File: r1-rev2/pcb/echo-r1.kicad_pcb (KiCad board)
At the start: 6 copper layers, 55 x 95 mm, 0 parts

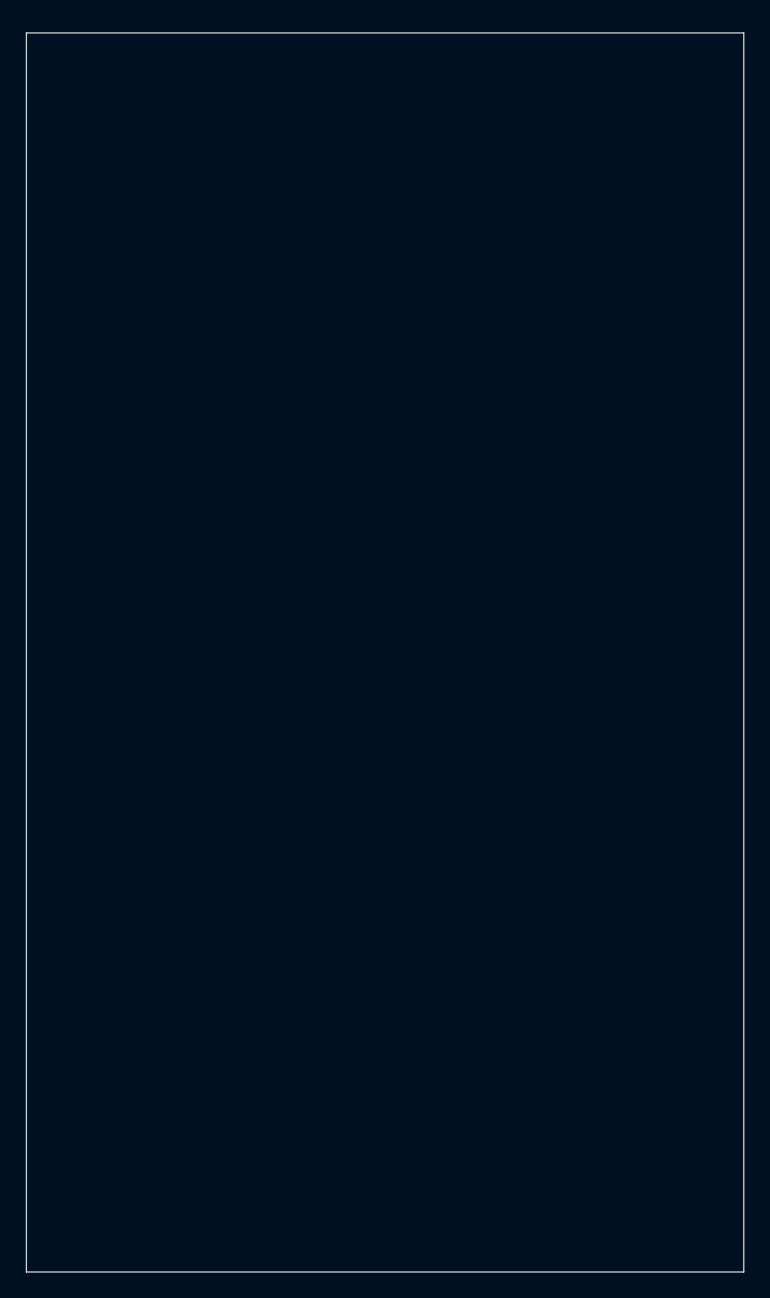
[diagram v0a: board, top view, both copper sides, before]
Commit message: R1-Rev2: update PCB stackup and board outline
The new board stackup uses alternate signal and ground layers,
being careful not to cross thicker cores. This should keep the
electric fields smaller, and in theory, is better for EMI than
the old stackup which didn't pay attention to the space between
layers. Power will be routed on signal layers.

The board outline is now rounded generously for compatibility
with CNC machined cases (which require rounded inner corners).
It is also now toleranced back from the inner edge of the case,
but I may pull it back further still.

There were some minor disreprancies from the intended JLC stackup
which have also been fixed, not that it really matters since KiCAD
doesn't use those values.
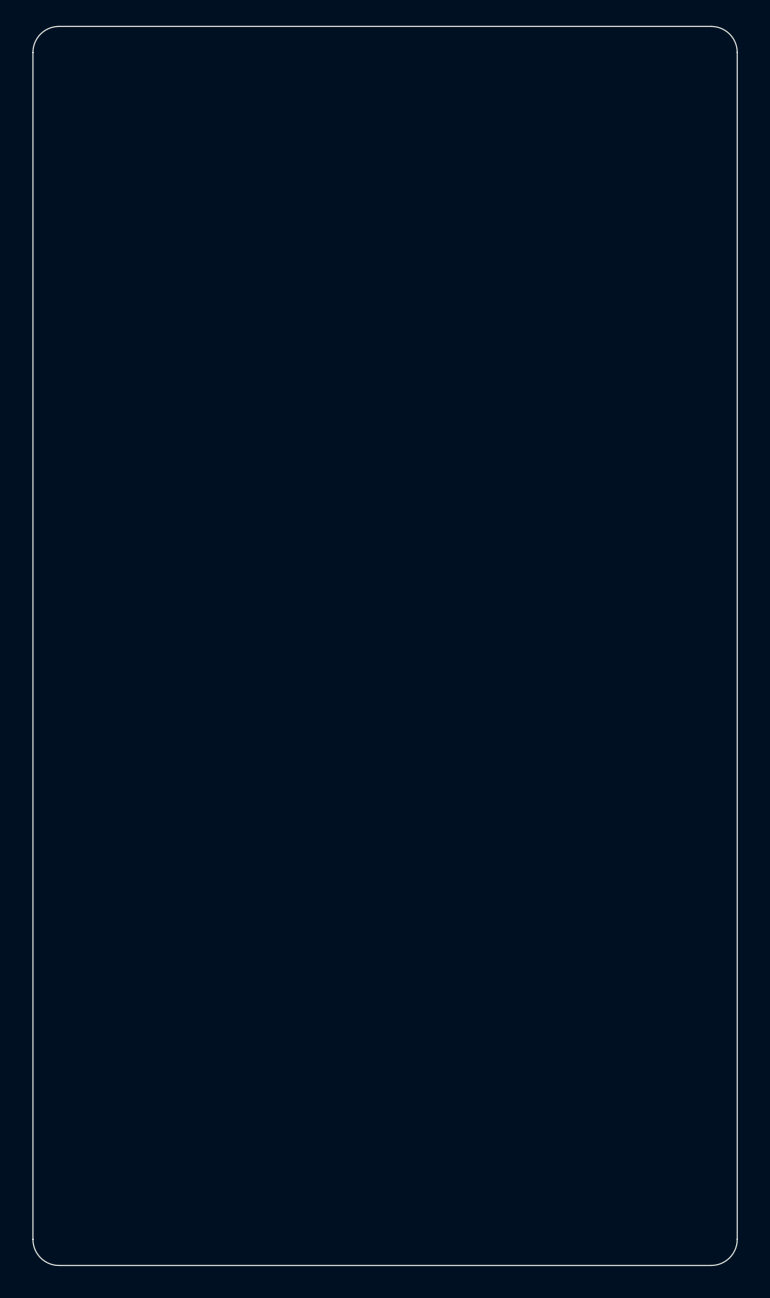
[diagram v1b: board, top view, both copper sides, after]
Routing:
- added copper zone on In2.Cu, net GND
- removed copper zone on In2.Cu, net (none)
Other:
- board size 55 x 95 mm -> 54 x 95 mm
- board text added: "Stackup: JLC06101H-3313, 1mm"
- board text removed: "Stackup: JLC06101H-3313"
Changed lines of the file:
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@@
 	(generator_version "9.0")
 	(general
-		(thickness 1.0524)
+		(thickness 1.06)
 		(legacy_teardrops no)
 	)
 	(paper "A4")
 	(layers
-		(0 "F.Cu" signal)
+		(0 "F.Cu" mixed)
 		(4 "In1.Cu" power "F.Gnd")
-		(6 "In2.Cu" power "F.Pwr")
-		(8 "In3.Cu" mixed "B.Inner")
+		(6 "In2.Cu" power "I.Gnd")
+		(8 "In3.Cu" mixed "I.Cu")
 		(10 "In4.Cu" power "B.Gnd")
-		(2 "B.Cu" signal)
+		(2 "B.Cu" mixed)
 		(9 "F.Adhes" user "F.Adhesive")
 		(11 "B.Adhes" user "B.Adhesive")
@@
 				(thickness 0.0994)
 				(material "3313*1")
-				(epsilon_r 4.5)
+				(epsilon_r 4.1)
 				(loss_tangent 0.02)
 			)
@@
 			(layer "dielectric 3"
 				(type "prepreg")
-				(thickness 0.2028)
+				(thickness 0.2104)
 				(material "7268*1")
 				(epsilon_r 4.5)
@@
 				(thickness 0.0994)
 				(material "3313*1")
-				(epsilon_r 4.5)
+				(epsilon_r 4.1)
 				(loss_tangent 0.02)
 			)
@@
 		(allow_soldermask_bridges_in_footprints no)
 		(tenting front back)
-		(aux_axis_origin 121 152.5)
-		(grid_origin 121 152.5)
+		(aux_axis_origin 121.5 152)
+		(grid_origin 121.5 152)
 		(pcbplotparams
 			(layerselection 0x00000000_00000000_55555555_5755f5ff)
@@
 	(net 1 "GND")
 	(gr_rect
-		(start 118.5 55)
-		(end 178.5 155)
+		(start 121 56.5)
+		(end 176 152.5)
 		(stroke
 			(width 0.1)
-			(type default)
+			(type solid)
 		)
 		(fill no)
@@
 	)
 	(gr_rect
-		(start 121 57.5)
-		(end 176 152.5)
-		(stroke
-			(width 0.05)
-			(type default)
+		(start 118.5 54.5)
+		(end 178.5 154.5)
+		(stroke
+			(width 0.1)
+			(type solid)
 		)
 		(fill no)
-		(layer "Edge.Cuts")
-	)
-	(gr_text "Stackup: JLC06101H-3313"
+		(layer "Dwgs.User")
+	)
+	(gr_arc
+		(start 121.5 59)
+		(mid 122.085786 57.585786)
+		(end 123.5 57)
+		(stroke
+			(width 0.05)
+			(type default)
+		)
+		(layer "Edge.Cuts")
+	)
+	(gr_arc
+		(start 123.5 152)
+		(mid 122.085786 151.414214)
+		(end 121.5 150)
+		(stroke
+			(width 0.05)
+			(type default)
+		)
+		(layer "Edge.Cuts")
+	)
+	(gr_line
+		(start 121.5 59)
+		(end 121.5 150)
+		(stroke
+			(width 0.05)
+			(type default)
+		)
+		(layer "Edge.Cuts")
+	)
+	(gr_line
+		(start 173.5 57)
+		(end 123.5 57)
+		(stroke
+			(width 0.05)
+			(type default)
+		)
+		(layer "Edge.Cuts")
+	)
+	(gr_arc
+		(start 173.5 57)
+		(mid 174.914214 57.585786)
+		(end 175.5 59)
+		(stroke
+			(width 0.05)
+			(type default)
+		)
+		(layer "Edge.Cuts")
+	)
+	(gr_line
+		(start 175.499999 150)
+		(end 175.5 59)
+		(stroke
+			(width 0.05)
+			(type default)
+		)
+		(layer "Edge.Cuts")
+	)
+	(gr_arc
+		(start 175.499999 150)
+		(mid 174.914213 151.414214)
+		(end 173.499999 152)
+		(stroke
+			(width 0.05)
+			(type default)
+		)
+		(layer "Edge.Cuts")
+	)
+	(gr_line
+		(start 123.5 152)
+		(end 173.5 152)
+		(stroke
+			(width 0.05)
+			(type default)
+		)
+		(layer "Edge.Cuts")
+	)
+	(gr_text "Stackup: JLC06101H-3313, 1mm"
 		(at 118.75 53.5 0)
 		(layer "Cmts.User")
@@
 		(net 1)
 		(net_name "GND")
-		(layers "In1.Cu" "In4.Cu")
+		(layers "In1.Cu" "In2.Cu" "In4.Cu")
 		(hatch edge 0.5)
 		(priority 1)
@@
 		(polygon
 			(pts
-				(xy 121 57.5) (xy 176 57.5) (xy 176 152.5) (xy 121 152.5)
-			)
-		)
-	)
-	(zone
-		(net 0)
-		(net_name "")
-		(layer "In2.Cu")
-		(hatch edge 0.5)
-		(priority 14)
-		(connect_pads yes
-			(clearance 0.25)
-		)
-		(min_thickness 0.25)
-		(filled_areas_thickness no)
-		(fill
-			(thermal_gap 0.5)
-			(thermal_bridge_width 0.5)
-		)
-		(polygon
-			(pts
-				(xy 121 57.5) (xy 176 57.5) (xy 176 152.5) (xy 121 152.5)
-			)
-		)
+				(xy 121.5 57) (xy 175.5 57) (xy 175.5 152) (xy 121.5 152)
+			)
+		)

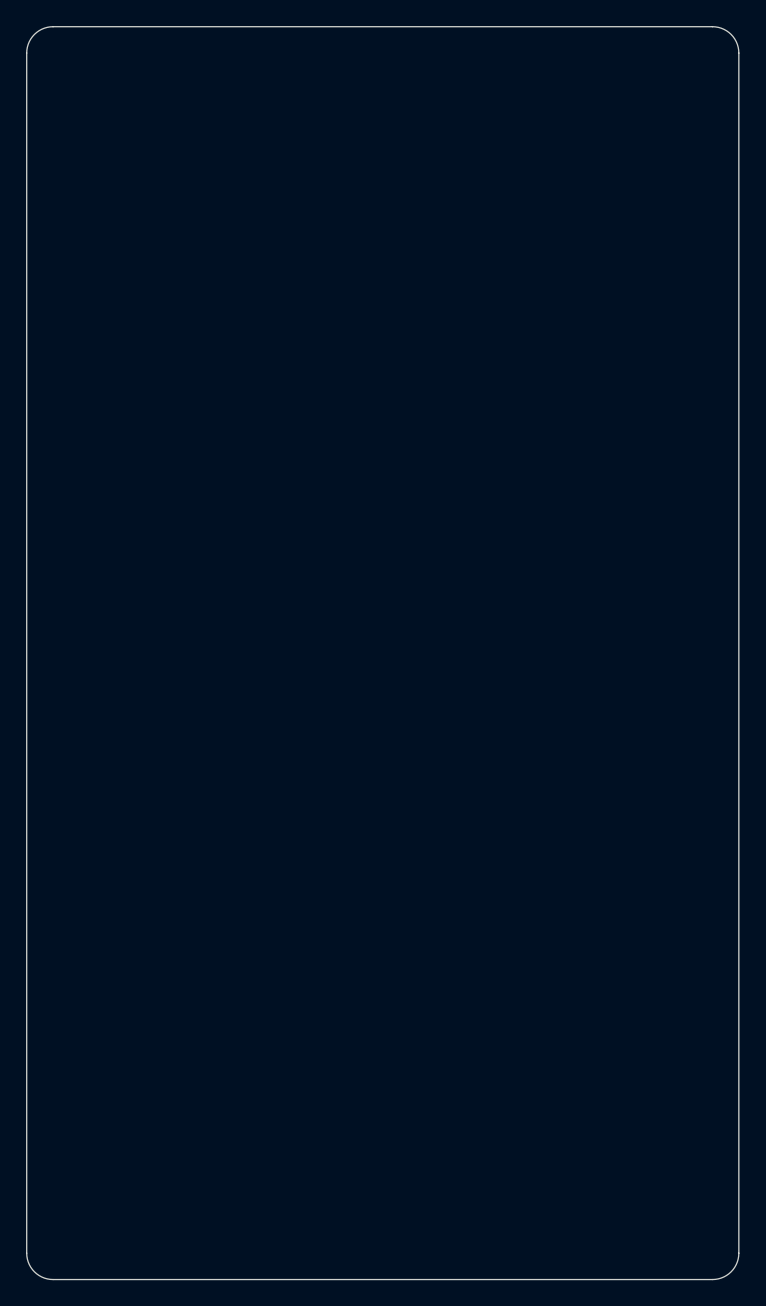
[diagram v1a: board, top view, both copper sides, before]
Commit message: R1-Rev2: initial mechanical layout
- Outline front side of case, LCD module, and cable
- Lay out LCD, since it requires 12'oclock viewing angle a slot is
  required to thread the ribbon cable through to the back plane.
- Place buttons, HP/LO jacks, and USB port
- Make the power/volume buttons larger
- Remove old button footprints
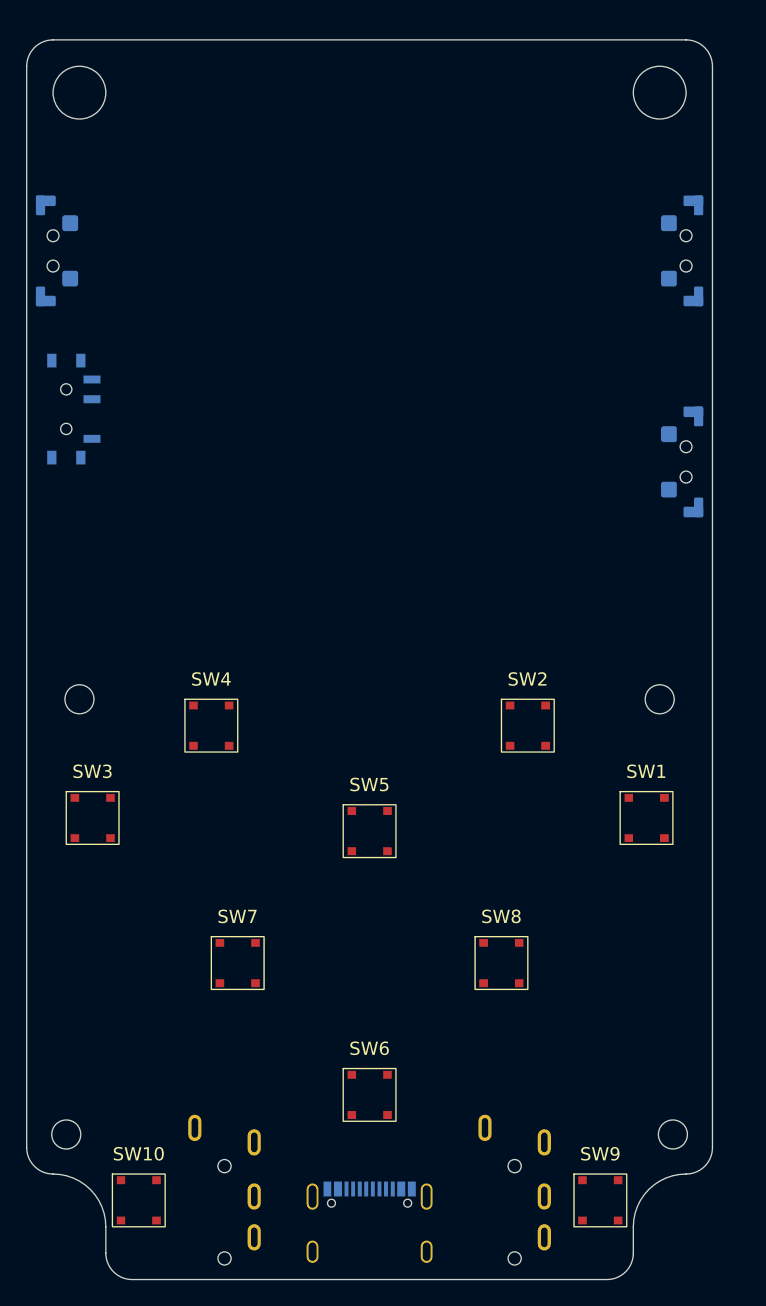
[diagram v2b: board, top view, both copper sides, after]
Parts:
- added H1: M2x2mm, MountingHole:MountingHole_2.2mm_M2, B.Cu at (125.5, 108.0)
- added H2: M2x2mm, MountingHole:MountingHole_2.2mm_M2, B.Cu at (169.5, 108.0)
- added H3: M2x2mm, MountingHole:MountingHole_2.2mm_M2, B.Cu at (170.5, 141.0)
- added H4: M2x2mm, MountingHole:MountingHole_2.2mm_M2, B.Cu at (124.5, 141.0)
- added H5: 4mm, MountingHole:MountingHole_4mm, B.Cu at (169.5, 62.0)
- added H6: 4mm, MountingHole:MountingHole_4mm, B.Cu at (125.5, 62.0)
- added H7: 18x2mm, echoplayer:Slot_18x2mm, B.Cu at (147.5, 86.0)
- added J2: TYPE-C-31-M-12, echoplayer:USB_C-Hroparts-TYPE-C-31-M-12, B.Cu at (147.5, 146.2)
- added J4: HP_3.5mm, echoplayer:Jack_3.5mm_HCTL_HC-PJ-320A-4P-D, B.Cu at (136.5, 147.0)
- added J5: LO_3.5mm, echoplayer:Jack_3.5mm_HCTL_HC-PJ-320A-4P-D, B.Cu at (158.5, 147.0)
- added SW1: A, echoplayer:Switch_SHOUHAN_TS3735PA, F.Cu at (168.5, 117.0)
- added SW10: SELECT, echoplayer:Switch_SHOUHAN_TS3735PA, F.Cu at (130.0, 146.0)
- added SW11: VOL+, echoplayer:Switch_HROPARTS_K2-1112SA-A4DW-01, B.Cu at (171.5, 74.0)
- added SW12: VOL-, echoplayer:Switch_HROPARTS_K2-1112SA-A4DW-01, B.Cu at (171.5, 90.0)
- added SW13: POWER, echoplayer:Switch_HROPARTS_K2-1112SA-A4DW-01, B.Cu at (123.5, 74.0)
- added SW14: HOLD, echoplayer:Switch_SHOUHAN_MSK12C02-HB, B.Cu at (124.5, 86.0)
- added SW2: B, echoplayer:Switch_SHOUHAN_TS3735PA, F.Cu at (159.5, 110.0)
- added SW3: X, echoplayer:Switch_SHOUHAN_TS3735PA, F.Cu at (126.5, 117.0)
- added SW4: Y, echoplayer:Switch_SHOUHAN_TS3735PA, F.Cu at (135.5, 110.0)
- added SW5: DPAD↑, echoplayer:Switch_SHOUHAN_TS3735PA, F.Cu at (147.5, 118.0)
- added SW6: DPAD↓, echoplayer:Switch_SHOUHAN_TS3735PA, F.Cu at (147.5, 138.0)
- added SW7: DPAD←, echoplayer:Switch_SHOUHAN_TS3735PA, F.Cu at (137.5, 128.0)
- added SW8: DPAD→, echoplayer:Switch_SHOUHAN_TS3735PA, F.Cu at (157.5, 128.0)
- added SW9: START, echoplayer:Switch_SHOUHAN_TS3735PA, F.Cu at (165.0, 146.0)
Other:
- board size 54 x 95 mm -> 52 x 94 mm
- board text added: "ACTIVE AREA"
- board text added: "BEND ZONE"
- board text added: "BEZEL LINE"
- board text added: "LCD MODULE"

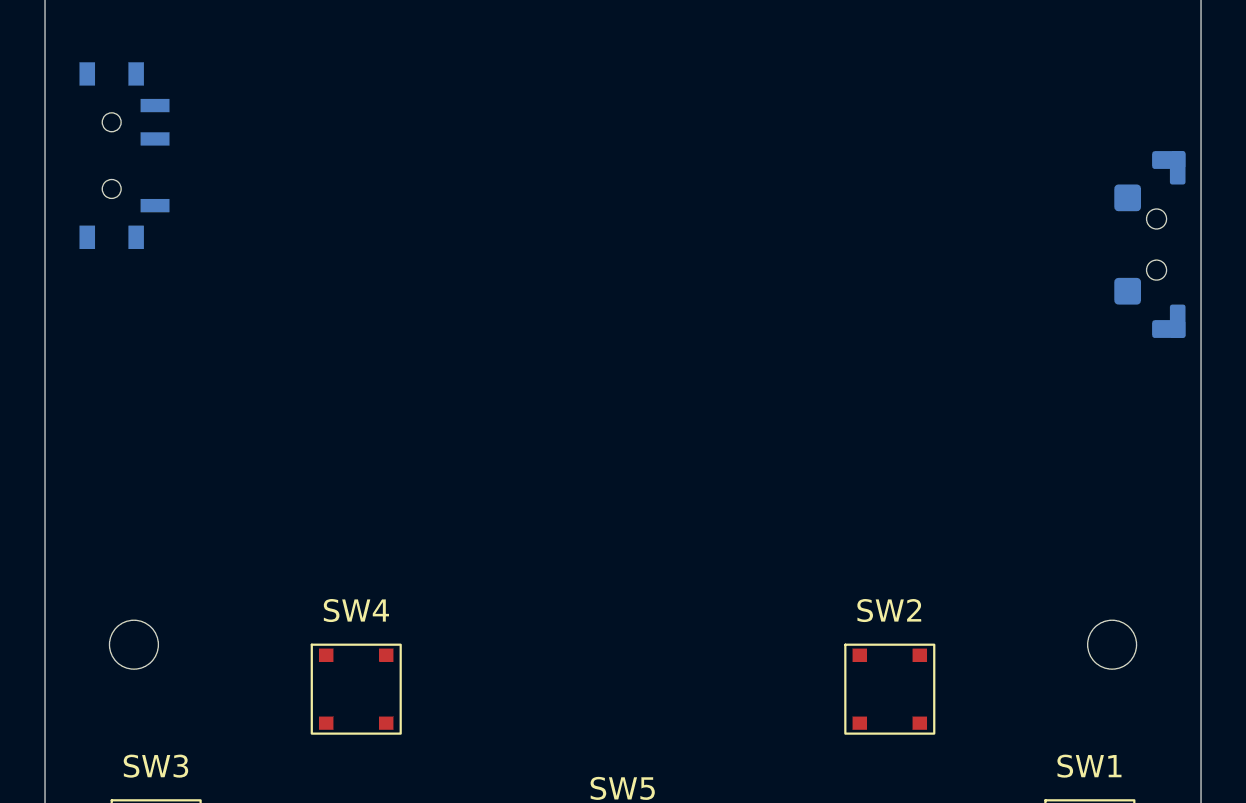
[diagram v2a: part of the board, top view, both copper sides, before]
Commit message: R1-Rev2: change LCD ribbon cable slot placement and size
The LCD won't sit flat if the fat side of the cable is lying
underneath it because there are a bunch of capacitors there.
The cable is long enough to reach the back of the PCB though
if the entire thing is put through a slot right underneath
the screen, although it's annoyingly huge.

I've removed the screw holes there since the routing becomes
very tight in that area with them in place. Depending on how
it goes there might be room to bring one of them back or put
a screw in the middle, between the slot and the D-pad.
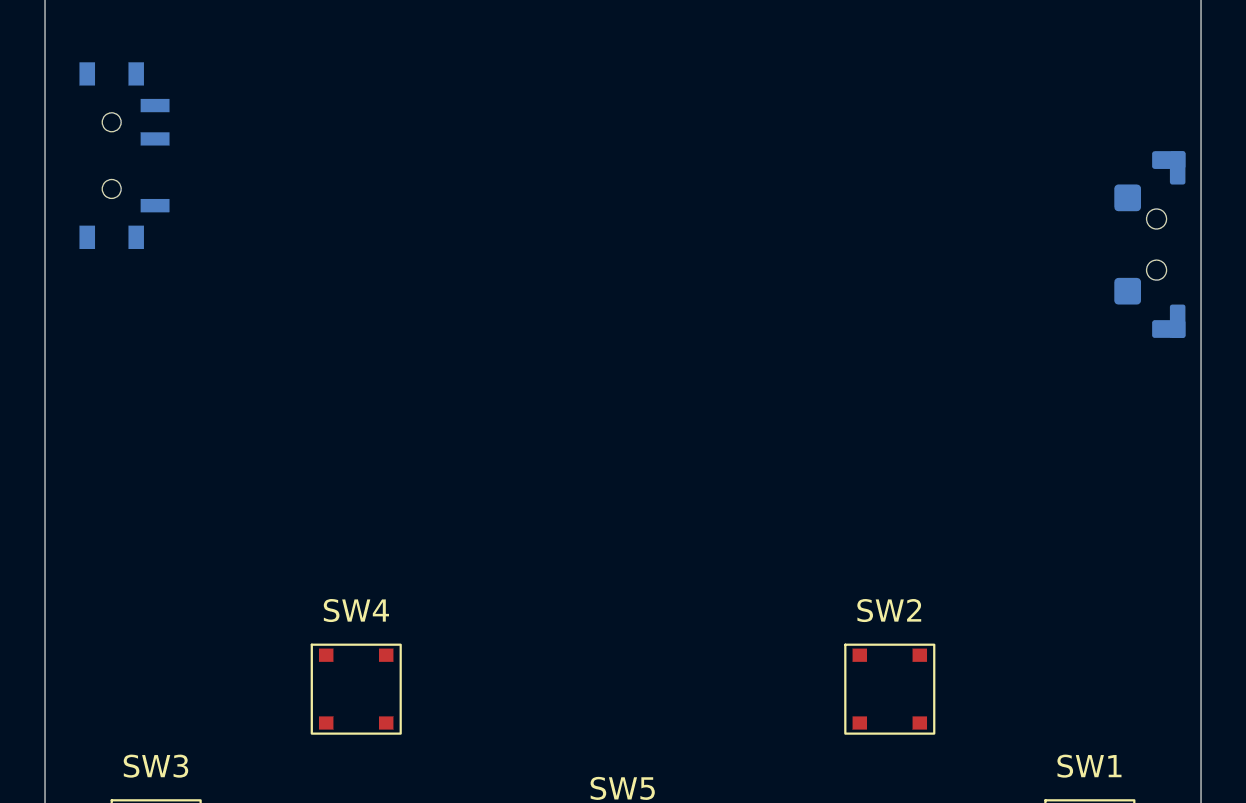
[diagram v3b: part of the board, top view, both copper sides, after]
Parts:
- removed the H1 at (125.5, 108.0)
- removed the H2 at (169.5, 108.0)
- H5: renamed from H7; value 18x2mm -> 38x2mm; footprint echoplayer:Slot_18x2mm -> echoplayer:Slot_38x2mm
- moved H5 18.0 mm to (147.5, 104.0), turned to 180 degrees
- renumbered H3 to H1, H4 to H2, H6 to H3, H5 to H4
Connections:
- net +3V3_LDO renamed +3V0_VBAT
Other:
- board text removed: "BEND ZONE"
